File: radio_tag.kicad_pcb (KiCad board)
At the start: 2 copper layers, 20 parts, among them J1 Conn_01x01, J2 Conn_01x01, J3 Conn_01x01, U1 TLV740P, U2 MICRF113, Y1 9M84375

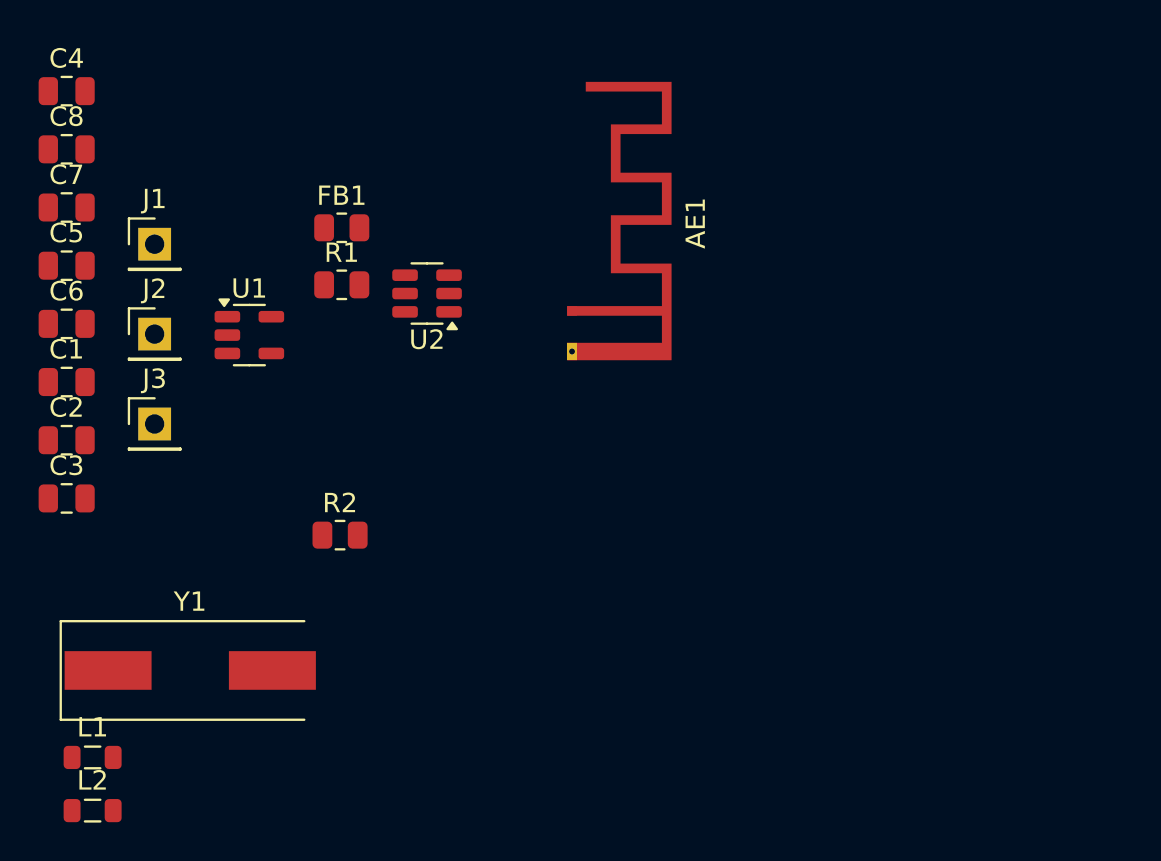
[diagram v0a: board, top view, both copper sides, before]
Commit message: Rough out component positions, remove incorrect antenna
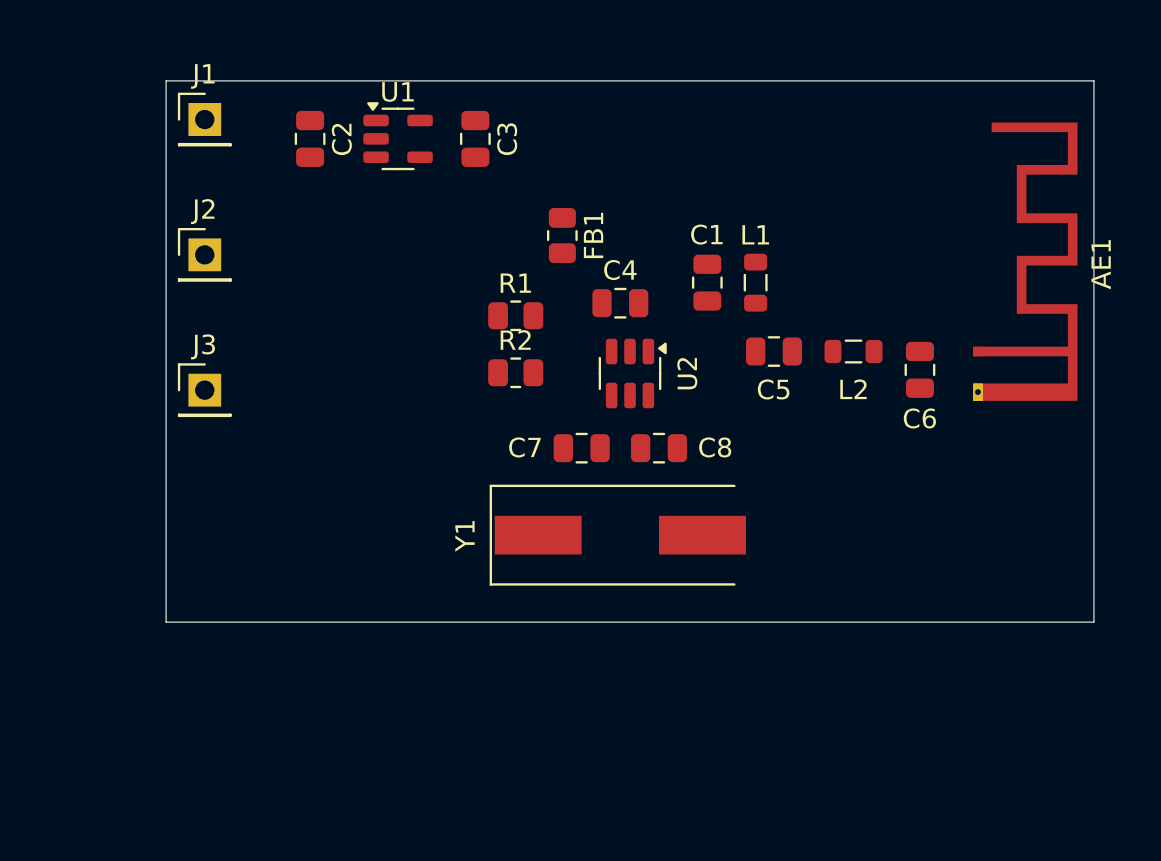
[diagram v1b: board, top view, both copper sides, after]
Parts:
- moved L2 46.0 mm to (204.6, 95.0)
- moved C6 44.2 mm to (208.0, 96.0), turned to -90 degrees
- moved L1 42.2 mm to (199.5, 91.4), turned to -90 degrees
- moved C5 36.9 mm to (200.4, 95.0)
- moved C8 34.3 mm to (194.5, 100.0), turned to 180 degrees
- moved C1 33.5 mm to (197.0, 91.4), turned to -90 degrees
- moved C4 30.7 mm to (192.5, 92.5)
- moved C7 29.4 mm to (190.5, 100.0)
- moved C3 28.2 mm to (185.0, 84.0), turned to -90 degrees
- moved Y1 23.3 mm to (192.5, 104.5)
- moved AE1 21.1 mm to (211.0, 95.0)
- moved C2 20.0 mm to (176.4, 84.0), turned to -90 degrees
- moved U1 12.7 mm to (181.0, 84.0)
- moved R2 12.4 mm to (187.1, 96.1)
- moved FB1 11.4 mm to (189.5, 89.0), turned to -90 degrees
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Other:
- board outline added: 48 x 28 mm

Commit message: Switch component values for 433 MHz operation
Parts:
- C5: value 10p -> 12p
- C6: value 6p8 -> 4p7
- L2: value 150n -> 68n
- Y1: value 9M84375 -> 13M560
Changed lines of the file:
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@@
 			)
 		)
-		(property "Value" "6p8"
+		(property "Value" "4p7"
 			(at 0 1.68 90)
 			(layer "F.Fab")
@@
 			)
 		)
-		(property "Manufacturer" "YAGEO"
+		(property "Manufacturer" "Cal-Chip Electronics"
 			(at 0 0 -90)
 			(unlocked yes)
@@
 			)
 		)
-		(property "Manufacturer PN" "CC0805CRNPO9BN6R8"
+		(property "Manufacturer PN" "CHV0805N2504R7CCT"
 			(at 0 0 -90)
 			(unlocked yes)
@@
 			)
 		)
-		(property "Supplier PN" "311-1831-1-ND"
+		(property "Supplier PN" "4713-CHV0805N2504R7CCT-ND"
 			(at 0 0 -90)
 			(unlocked yes)
@@
 			)
 		)
-		(property "Value" "10p"
+		(property "Value" "12p"
 			(at 0 1.68 0)
 			(layer "F.Fab")
@@
 			)
 		)
-		(property "Manufacturer" "Samsung Electro-mechanics"
-			(at 0 0 0)
-			(unlocked yes)
-			(layer "F.Fab")
-			(hide yes)
-			(effects
-				(font
-					(size 1 1)
-					(thickness 0.15)
-				)
-			)
-		)
-		(property "Manufacturer PN" "CL21C100CBANNNC"
-			(at 0 0 0)
-			(unlocked yes)
-			(layer "F.Fab")
-			(hide yes)
-			(effects
-				(font
-					(size 1 1)
-					(thickness 0.15)
-				)
-			)
-		)
-		(property "Supplier PN" "1276-2561-1-ND"
+		(property "Manufacturer" "Cal-Chip Electronics"
+			(at 0 0 0)
+			(unlocked yes)
+			(layer "F.Fab")
+			(hide yes)
+			(effects
+				(font
+					(size 1 1)
+					(thickness 0.15)
+				)
+			)
+		)
+		(property "Manufacturer PN" "CHV0805N250120FCT"
+			(at 0 0 0)
+			(unlocked yes)
+			(layer "F.Fab")
+			(hide yes)
+			(effects
+				(font
+					(size 1 1)
+					(thickness 0.15)
+				)
+			)
+		)
+		(property "Supplier PN" "4713-CHV0805N250120FCT-ND"
 			(at 0 0 0)
 			(unlocked yes)
@@
 			)
 		)
-		(property "Value" "9M84375"
+		(property "Value" "13M560"
 			(at 0 3.55 0)
 			(layer "F.Fab")
@@
 			)
 		)
-		(property "Manufacturer" "ECS"
-			(at 0 0 0)
-			(unlocked yes)
-			(layer "F.Fab")
-			(hide yes)
-			(effects
-				(font
-					(size 1 1)
-					(thickness 0.15)
-				)
-			)
-		)
-		(property "Manufacturer PN" "ECS-98.4375-CDX-0314-TR"
+		(property "Manufacturer" "Abracon"
+			(at 0 0 0)
+			(unlocked yes)
+			(layer "F.Fab")
+			(hide yes)
+			(effects
+				(font
+					(size 1 1)
+					(thickness 0.15)
+				)
+			)
+		)
+		(property "Manufacturer PN" "ABLS-13.560MHZ-10-R20-D-T"
 			(at 0 0 0)
 			(unlocked yes)
@@
 			)
 		)
-		(property "Supplier PN" "XC1026CT-ND"
+		(property "Supplier PN" "535-9687-1-ND"
 			(at 0 0 0)
 			(unlocked yes)
@@
 			)
 		)
-		(property "Value" "150n"
+		(property "Value" "68n"
 			(at 0 1.55 0)
 			(layer "F.Fab")
@@
 			)
 		)
-		(property "Manufacturer" "Pulse Electronics"
-			(at 0 0 0)
-			(unlocked yes)
-			(layer "F.Fab")
-			(hide yes)
-			(effects
-				(font
-					(size 1 1)
-					(thickness 0.15)
-				)
-			)
-		)
-		(property "Manufacturer PN" "BSCH00100505R15JCS"
-			(at 0 0 0)
-			(unlocked yes)
-			(layer "F.Fab")
-			(hide yes)
-			(effects
-				(font
-					(size 1 1)
-					(thickness 0.15)
-				)
-			)
-		)
-		(property "Supplier PN" "553-BSCH00100505R15JCSCT-ND"
-			(at 0 0 0)
-			(unlocked yes)
+		(property "Manufacturer" "Johanson Technology"
+			(at 0 0 0)
+			(unlocked yes)
+			(layer "F.Fab")
+			(hide yes)
+			(effects
+				(font
+					(size 1 1)
+					(thickness 0.15)
+				)
+			)
+		)
+		(property "Manufacturer PN" "LRC0603CJ68NGV001T"
+			(at 0 0 0)
+			(unlocked yes)
+			(layer "F.Fab")
+			(hide yes)
+			(effects
+				(font
+					(size 1 1)
+					(thickness 0.15)
+				)
+			)
+		)
+		(property "Supplier PN" "712-LRC0603CJ68NGV001TCT-ND"
+			(at 0 0 0)
+			(unlocked yes)

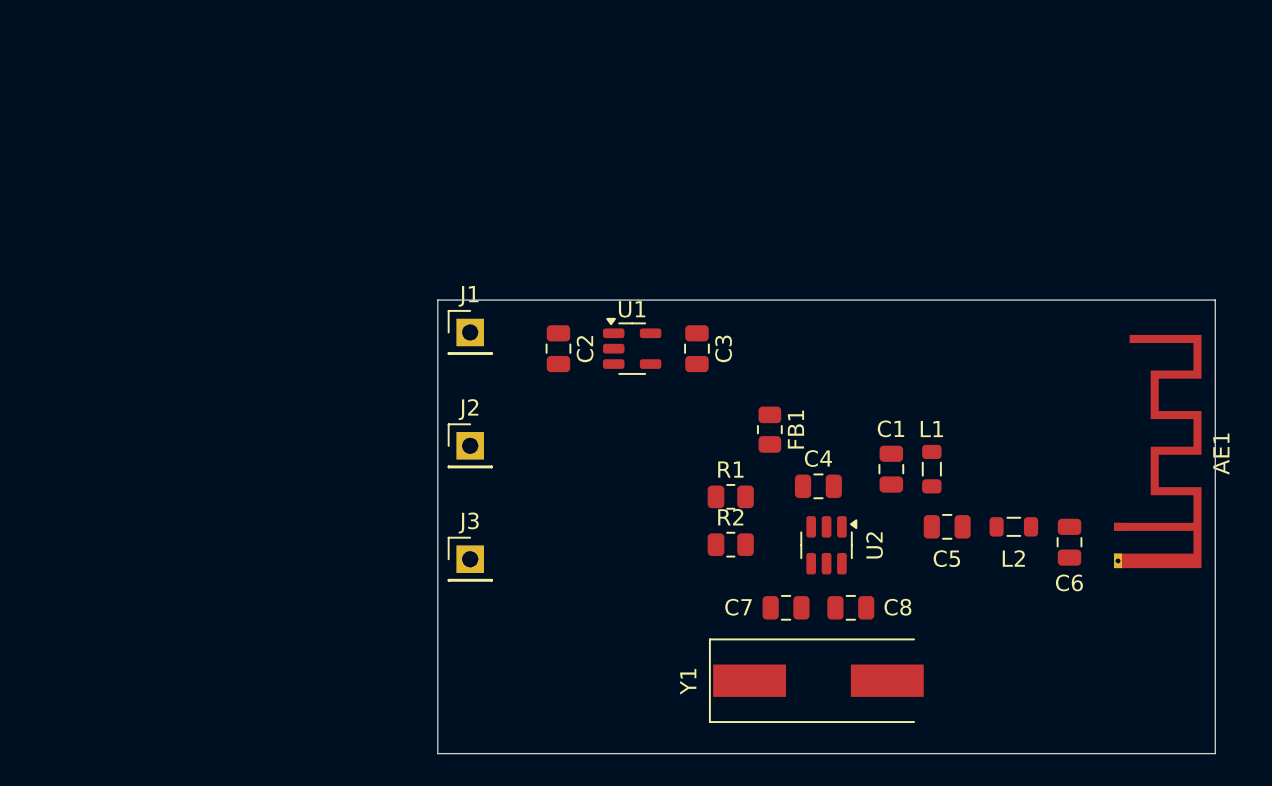
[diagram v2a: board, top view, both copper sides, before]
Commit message: Select new antenna and add to layout
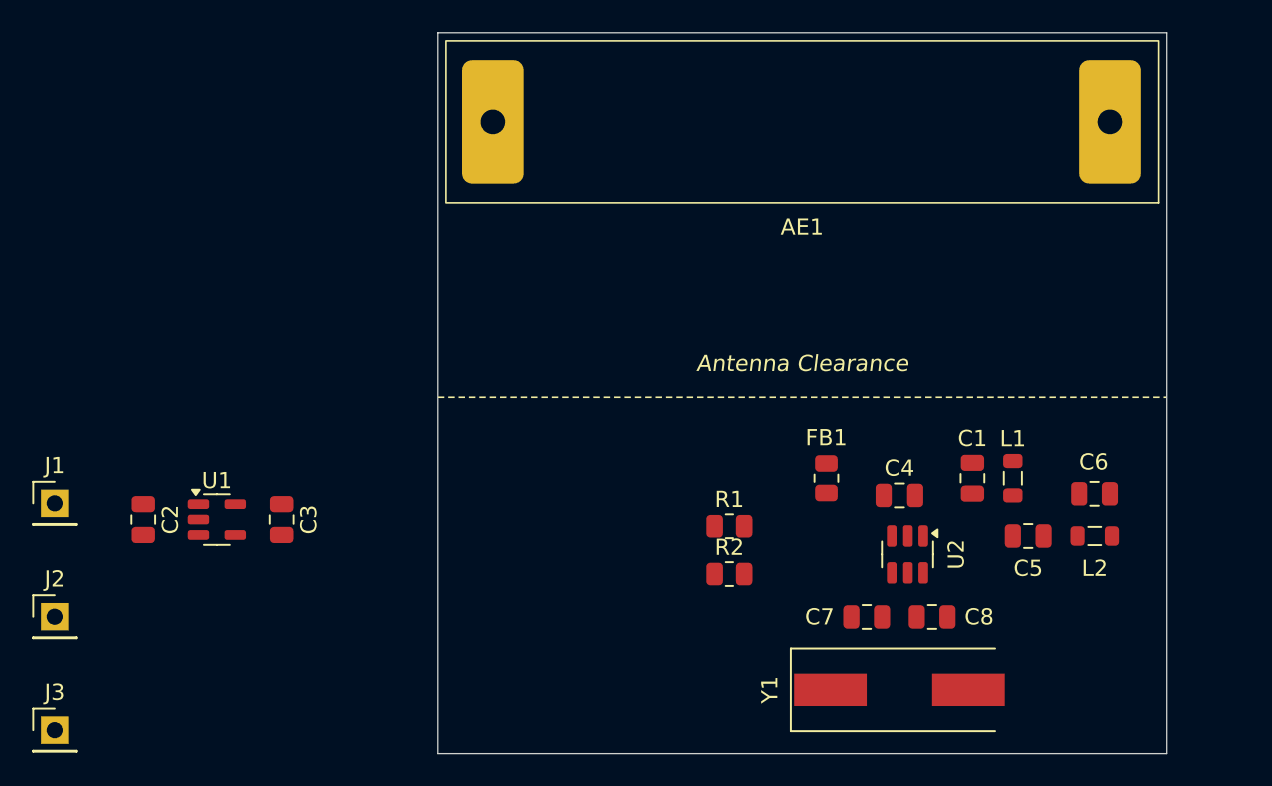
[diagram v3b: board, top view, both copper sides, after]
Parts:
- AE1: footprint RF_Antenna:Texas_SWRA117D_2.4GHz_Left -> rf:TE_ANT-433-HETH
- moved C2 27.7 mm to (150.8, 94.5)
- moved C3 27.7 mm to (159.4, 94.5)
- moved J1 27.7 mm to (145.4, 93.5)
- moved J2 27.7 mm to (145.4, 100.5)
- moved J3 27.7 mm to (145.4, 107.5)
- moved U1 27.7 mm to (155.4, 94.5)
- moved AE1 25.0 mm to (210.5, 70.0), turned to 180 degrees
- moved C1 5.03 mm to (202.0, 92.0)
- moved C4 5.03 mm to (197.5, 93.1)
- moved C5 5.03 mm to (205.4, 95.6)
- moved C7 5.03 mm to (195.5, 100.6)
- moved C8 5.03 mm to (199.5, 100.6)
- moved L1 5.03 mm to (204.5, 92.0)
- moved L2 5.03 mm to (209.6, 95.6)
- moved U2 5.03 mm to (198.0, 96.7)
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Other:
- board size 48 x 28 mm -> 45 x 44.5 mm
- board text added: "Antenna Clearance"

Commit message: Route PCB
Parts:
- moved C2 28.8 mm to (179.5, 92.5)
- moved C3 28.7 mm to (188.0, 92.5)
- moved U1 28.7 mm to (184.0, 92.5)
- moved J3 27.6 mm to (172.5, 102.5)
- moved J2 27.3 mm to (172.5, 97.5)
- moved J1 27.2 mm to (172.5, 92.5)
- moved R1 5.48 mm to (192.0, 97.2)
- moved AE1 2.50 mm to (208.0, 70.0)
- moved R2 1.02 mm to (188.0, 98.1), turned to 90 degrees
- moved C1 0.50 mm to (202.0, 92.5)
- moved C4 0.50 mm to (197.5, 93.6)
- moved C5 0.50 mm to (205.4, 96.1)
- moved C6 0.50 mm to (209.6, 93.5)
- moved C7 0.50 mm to (195.5, 101.1)
- moved C8 0.50 mm to (199.5, 101.1)
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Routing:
- net /TX_ANT: track 0.00 -> 27.1 mm
- net GND: track 0.00 -> 21.7 mm, vias 0 -> 8
- net /PWR_TX_3V3: track 0.00 -> 19.4 mm
- net /TX_IN: track 0.00 -> 18.7 mm
- net /PWR_IN: track 0.00 -> 14.7 mm
- net /TX_XTAL_IN: track 0.00 -> 10.4 mm
- net /TX_XTAL_OUT: track 0.00 -> 10.3 mm
- net /TX_OUT: track 0.00 -> 8.05 mm
- net /TX_ASK: track 0.00 -> 7.03 mm
- net /PWR_TX_INT: track 0.00 -> 6.32 mm
- net /TX_FILTER: track 0.00 -> 2.10 mm
- added copper zone on In1.Cu, net GND
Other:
- board size 45 x 44.5 mm -> 50 x 50 mm
- copper layers 2 -> 4
- rule pad_to_mask_clearance: 0 -> 0.038
- board text added: "5V"
- board text added: "DATA"
- board text added: "GND"
- board text added: "J. L. Hay"
- board text added: "MICRF113 Dev. Board"
- board text added: "MICRF133 Dev. Board"
- board text added: "Rev. A - 01/02/2025"

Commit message: Revise board to use SMA edge mount connector, mark as Rev. B
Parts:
- removed AE1: Antenna_Dipole, rf:TE_ANT-433-HETH
- added J4: SMA, Connector_Coaxial:SMA_Samtec_SMA-J-P-H-ST-EM1_EdgeMount, F.Cu at (222.0, 97.5)
- moved C6 4.95 mm to (213.0, 97.0), turned to -90 degrees
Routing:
- net /TX_ANT: track 27.1 -> 12.1 mm
- net GND: track 21.7 -> 27.1 mm, vias 8 -> 10
- added copper zone on B.Cu, net GND
- added copper zone on In2.Cu, net GND
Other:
- board size 50 x 50 mm -> 60 x 24 mm
- board text added: "(433 MHz)"
- board text added: "50Ω"
- board text added: "ANT"
- board text added: "Rev. B - 02/02/2025"
- board text removed: "Antenna Clearance"
- board text removed: "Rev. A - 01/02/2025"
